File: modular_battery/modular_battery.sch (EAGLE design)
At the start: 16 parts

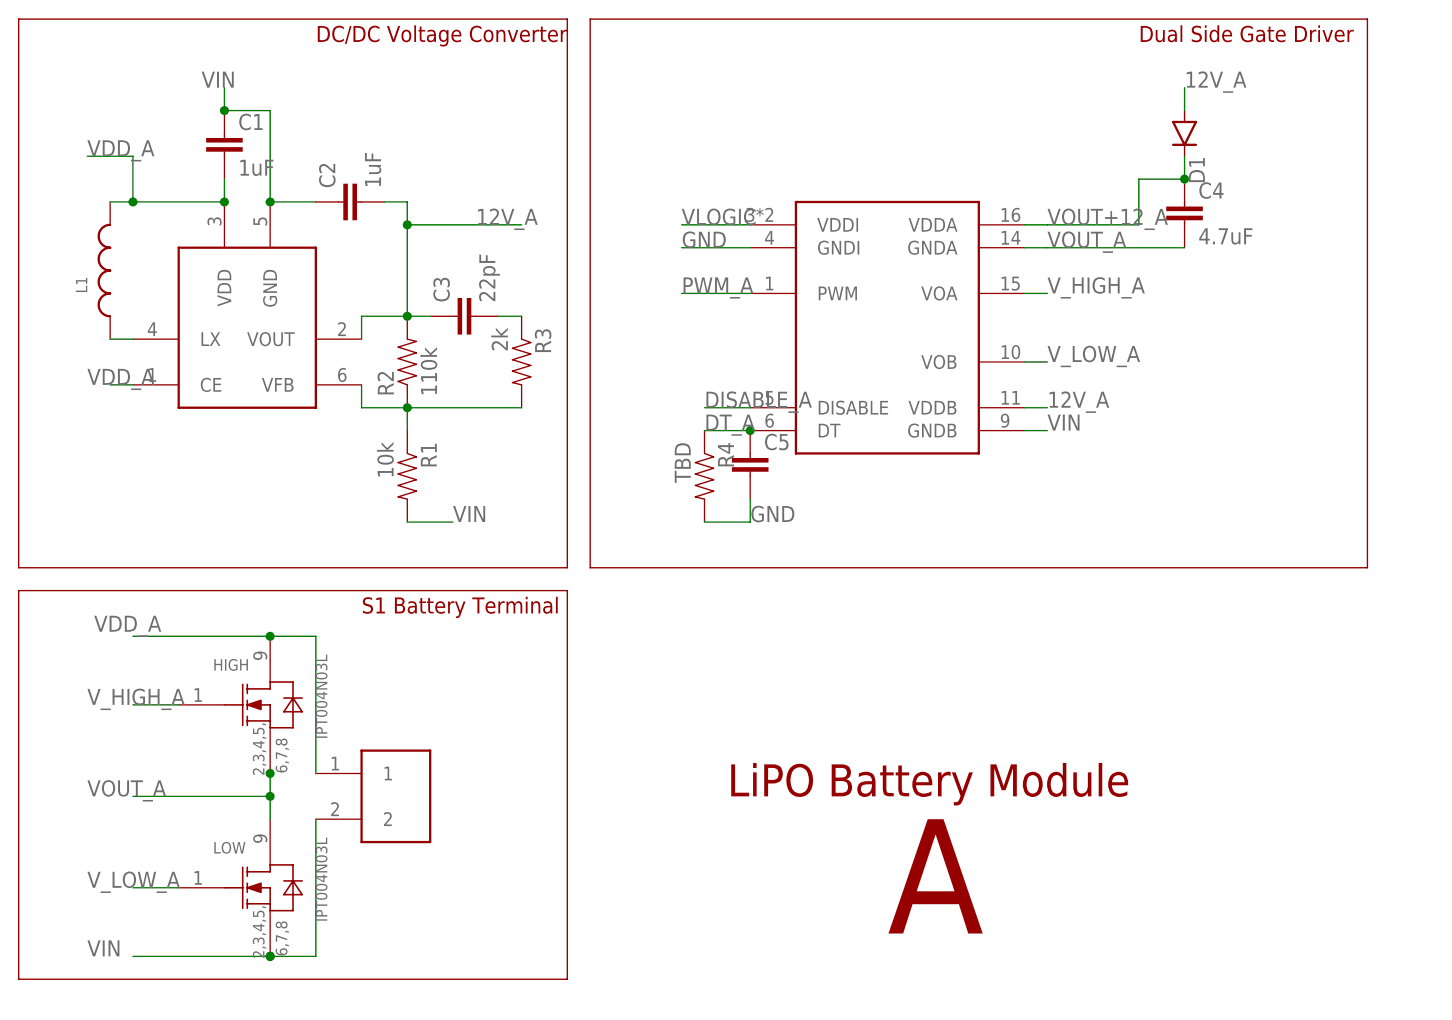
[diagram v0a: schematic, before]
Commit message: added UV supervisor - mosfets look good, copied to modular_battery schematic - i guess you need to recopy it back or something later
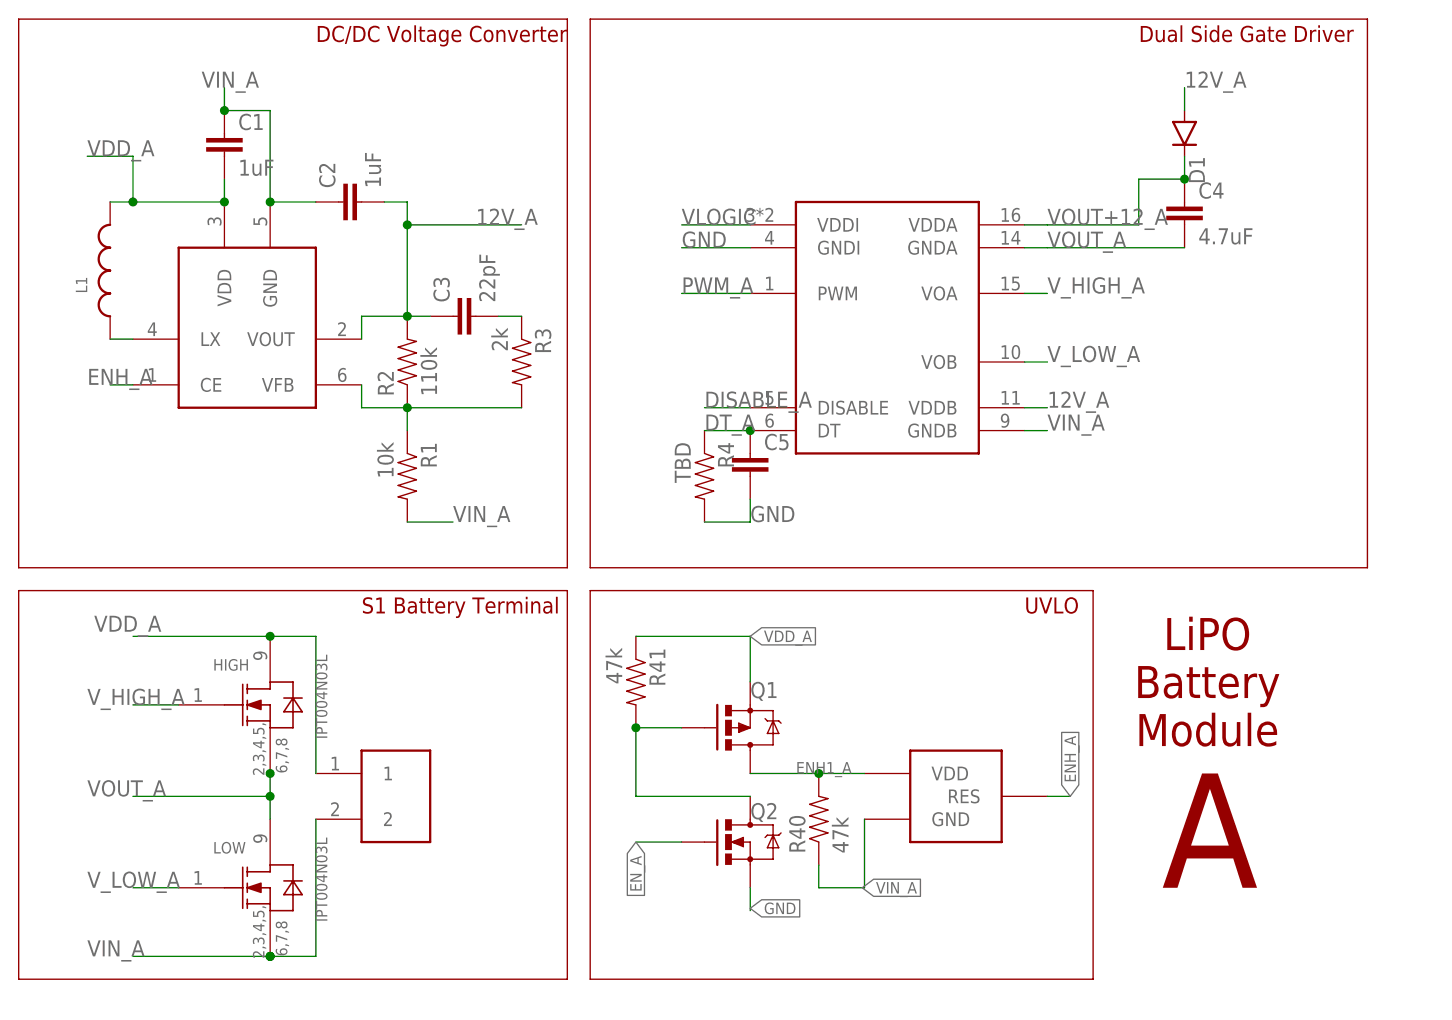
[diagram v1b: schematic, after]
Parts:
- added Q1: MOSFET-PCHANNELSOT223, Custom_old:MOSFET-PCHANNELSOT223
- added Q2: MOSFET-NCHANNELSMD, Custom_old:MOSFET-NCHANNELSMD
- added R40, R41: 47k, SparkFun-Passives:RESISTOR0603-RES
- added U$1: BD49XXK__G, Custom_old:BD49XXK__G
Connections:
- removed net VIN: C1.1, C2.1, LOW.2, LOW.3, LOW.4, LOW.5, LOW.6, LOW.7, LOW.8, R1.2, R1200.GND, SI823.GNDB, U$3.2
- new net ENH1_A: Q1.D, R40.2, U$1.VDD
- new net ENH_A: R1200.CE, U$1.RES
- new net EN_A: Q2.G
- new net N$26: Q1.G, Q2.D, R41.2
- new net VIN_A: C1.1, C2.1, LOW.2, LOW.3, LOW.4, LOW.5, LOW.6, LOW.7, LOW.8, R1.2, R1200.GND, R40.1, SI823.GNDB, U$1.GND, U$3.2
- net GND: now also Q2.S
- net VDD_A: now also Q1.S, R41.1; no longer R1200.CE
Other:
- note added: "UVLO"
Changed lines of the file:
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@@
 <?xml version="1.0" encoding="utf-8"?>
 <!DOCTYPE eagle SYSTEM "eagle.dtd">
-<eagle version="9.2.0">
+<eagle version="9.1.1">
 <drawing>
 <settings>
@@
 <layer number="56" name="wert" color="7" fill="1" visible="no" active="no"/>
 <layer number="57" name="tCAD" color="7" fill="1" visible="no" active="no"/>
+<layer number="59" name="tCarbon" color="7" fill="1" visible="no" active="no"/>
+<layer number="60" name="bCarbon" color="7" fill="1" visible="no" active="no"/>
 <layer number="88" name="SimResults" color="9" fill="1" visible="yes" active="yes"/>
 <layer number="89" name="SimProbes" color="9" fill="1" visible="yes" active="yes"/>
@@
 <layer number="112" name="tSilk" color="7" fill="1" visible="no" active="yes"/>
 <layer number="113" name="ReferenceLS" color="7" fill="1" visible="no" active="no"/>
+<layer number="114" name="Badge_Outline" color="7" fill="1" visible="no" active="yes"/>
+<layer number="115" name="ReferenceISLANDS" color="7" fill="1" visible="no" active="yes"/>
 <layer number="116" name="Patch_BOT" color="9" fill="4" visible="yes" active="yes"/>
+<layer number="117" name="BACKMAAT1" color="7" fill="1" visible="no" active="yes"/>
 <layer number="118" name="Rect_Pads" color="7" fill="1" visible="no" active="no"/>
+<layer number="119" name="KAP_TEKEN" color="7" fill="1" visible="no" active="yes"/>
+<layer number="120" name="KAP_MAAT1" color="7" fill="1" visible="no" active="yes"/>
 <layer number="121" name="_tsilk" color="7" fill="1" visible="yes" active="yes"/>
 <layer number="122" name="_bsilk" color="7" fill="1" visible="yes" active="yes"/>
@@
 <layer number="127" name="_tValues" color="7" fill="1" visible="no" active="yes"/>
 <layer number="128" name="_bValues" color="7" fill="1" visible="no" active="yes"/>
+<layer number="129" name="Mask" color="7" fill="1" visible="no" active="yes"/>
+<layer number="130" name="SMDSTROOK" color="7" fill="1" visible="no" active="yes"/>
 <layer number="131" name="tAdjust" color="7" fill="1" visible="no" active="yes"/>
 <layer number="132" name="bAdjust" color="7" fill="1" visible="no" active="yes"/>
+<layer number="133" name="bottom_silk" color="7" fill="1" visible="no" active="yes"/>
 <layer number="144" name="Drill_legend" color="7" fill="1" visible="yes" active="yes"/>
 <layer number="150" name="Notes" color="7" fill="1" visible="no" active="yes"/>
@@
 <layer number="223" name="223bmp" color="24" fill="1" visible="no" active="no"/>
 <layer number="224" name="224bmp" color="25" fill="1" visible="no" active="no"/>
+<layer number="225" name="225bmp" color="7" fill="1" visible="no" active="yes"/>
+<layer number="226" name="226bmp" color="7" fill="1" visible="no" active="yes"/>
+<layer number="227" name="227bmp" color="7" fill="1" visible="no" active="yes"/>
+<layer number="228" name="228bmp" color="7" fill="1" visible="no" active="yes"/>
+<layer number="229" name="229bmp" color="7" fill="1" visible="no" active="yes"/>
+<layer number="230" name="230bmp" color="7" fill="1" visible="no" active="yes"/>
 <layer number="231" name="Eagle3D_PG1" color="7" fill="1" visible="no" active="no"/>
 <layer number="232" name="Eagle3D_PG2" color="7" fill="1" visible="no" active="no"/>
@@
 <part name="C5" library="SparkFun-Passives" deviceset="CAP" device="0603-CAP"/>
 <part name="L1" library="PowerMagnetics (rev18e)" deviceset="WE-LQS_4025" device="" technology="_74404043220A"/>
+<part name="R40" library="SparkFun-Passives" deviceset="RESISTOR" device="0603-RES" value="47k"/>
+<part name="Q1" library="Custom_old" deviceset="MOSFET-PCHANNEL" device="SOT223"/>
+<part name="R41" library="SparkFun-Passives" deviceset="RESISTOR" device="0603-RES" value="47k"/>
+<part name="Q2" library="Custom_old" deviceset="MOSFET-NCHANNEL" device="SMD"/>
+<part name="U$1" library="Custom_old" deviceset="BD49XX" device="K__G"/>
 </parts>
 <sheets>
@@
 <wire x1="160.02" y1="116.84" x2="73.66" y2="116.84" width="0.1524" layer="94"/>
 <wire x1="73.66" y1="116.84" x2="73.66" y2="177.8" width="0.1524" layer="94"/>
-<text x="88.9" y="91.44" size="3.556" layer="94">LiPO Battery Module</text>
-<text x="106.68" y="76.2" size="12.7" layer="94">A</text>
+<text x="142.24" y="104.14" size="3.556" layer="94" align="center">LiPO
+Battery
+Module</text>
+<text x="137.16" y="81.28" size="12.7" layer="94">A</text>
+<wire x1="73.66" y1="114.3" x2="73.66" y2="71.12" width="0.1524" layer="94"/>
+<wire x1="73.66" y1="71.12" x2="129.54" y2="71.12" width="0.1524" layer="94"/>
+<wire x1="129.54" y1="71.12" x2="129.54" y2="114.3" width="0.1524" layer="94"/>
+<wire x1="129.54" y1="114.3" x2="73.66" y2="114.3" width="0.1524" layer="94"/>
+<text x="121.92" y="111.76" size="1.778" layer="94">UVLO</text>
 </plain>
 <instances>
@@
 <attribute name="VALUE" x="22.86" y="147.32" size="1.27" layer="96" rot="R90"/>
 </instance>
+<instance part="R40" gate="G$1" x="99.06" y="88.9" rot="R90">
+<attribute name="NAME" x="97.5614" y="85.09" size="1.778" layer="95" rot="R90"/>
+<attribute name="VALUE" x="102.362" y="85.09" size="1.778" layer="96" rot="R90"/>
+</instance>
+<instance part="Q1" gate="G$1" x="91.44" y="99.06" smashed="yes" rot="MR180">
+<attribute name="NAME" x="91.44" y="104.14" size="1.778" layer="95" rot="MR180"/>
+</instance>
+<instance part="R41" gate="G$1" x="78.74" y="104.14" rot="R270">
+<attribute name="NAME" x="80.2386" y="107.95" size="1.778" layer="95" rot="R270"/>
+<attribute name="VALUE" x="75.438" y="107.95" size="1.778" layer="96" rot="R270"/>
+</instance>
+<instance part="Q2" gate="G$1" x="91.44" y="86.36" smashed="yes">
+<attribute name="NAME" x="91.44" y="88.9" size="1.778" layer="95"/>
+</instance>
+<instance part="U$1" gate="G$1" x="114.3" y="91.44"/>
 </instances>
 <busses>
@@
 <wire x1="91.44" y1="121.92" x2="86.36" y2="121.92" width="0.1524" layer="91"/>
 <label x="91.44" y="121.92" size="1.778" layer="95"/>
+</segment>
+<segment>
+<pinref part="Q2" gate="G$1" pin="S"/>
+<wire x1="91.44" y1="81.28" x2="91.44" y2="78.74" width="0.1524" layer="91"/>
+<label x="91.44" y="78.994" size="1.27" layer="95" xref="yes"/>
 </segment>
 </net>
@@
 </segment>
 <segment>
-<pinref part="R1200" gate="G$1" pin="CE"/>
-<wire x1="22.86" y1="137.16" x2="20.32" y2="137.16" width="0.1524" layer="91"/>
-<label x="17.78" y="137.16" size="1.778" layer="95"/>
+<pinref part="Q1" gate="G$1" pin="S"/>
+<wire x1="91.44" y1="104.14" x2="91.44" y2="109.22" width="0.1524" layer="91"/>
+<label x="91.44" y="109.22" size="1.27" layer="95" xref="yes"/>
+<pinref part="R41" gate="G$1" pin="1"/>
+<wire x1="78.74" y1="109.22" x2="91.44" y2="109.22" width="0.1524" layer="91"/>
 </segment>
 </net>
@@
 </segment>
 </net>
-<net name="VIN" class="0">
+<net name="VIN_A" class="0">
 <segment>
 <wire x1="38.1" y1="73.66" x2="22.86" y2="73.66" width="0.1524" layer="91"/>
@@
 <junction x="38.1" y="157.48"/>
 </segment>
+<segment>
+<pinref part="R40" gate="G$1" pin="1"/>
+<wire x1="99.06" y1="83.82" x2="99.06" y2="81.28" width="0.1524" layer="91"/>
+<label x="103.886" y="81.28" size="1.27" layer="95" xref="yes"/>
+<pinref part="U$1" gate="G$1" pin="GND"/>
+<wire x1="104.14" y1="88.9" x2="104.14" y2="81.28" width="0.1524" layer="91"/>
+<wire x1="104.14" y1="81.28" x2="99.06" y2="81.28" width="0.1524" layer="91"/>
+</segment>
 </net>
 <net name="PWM_A" class="0">
@@
 </segment>
 </net>
+<net name="N$26" class="0">
+<segment>
+<pinref part="R41" gate="G$1" pin="2"/>
+<pinref part="Q1" gate="G$1" pin="G"/>
+<wire x1="78.74" y1="99.06" x2="83.82" y2="99.06" width="0.1524" layer="91"/>
+<pinref part="Q2" gate="G$1" pin="D"/>
+<wire x1="91.44" y1="91.44" x2="78.74" y2="91.44" width="0.1524" layer="91"/>
+<wire x1="78.74" y1="91.44" x2="78.74" y2="99.06" width="0.1524" layer="91"/>
+<junction x="78.74" y="99.06"/>
+</segment>
+</net>
+<net name="EN_A" class="0">
+<segment>
+<pinref part="Q2" gate="G$1" pin="G"/>
+<wire x1="83.82" y1="86.36" x2="78.74" y2="86.36" width="0.1524" layer="91"/>
+<label x="78.74" y="86.36" size="1.27" layer="95" rot="R270" xref="yes"/>
+</segment>
+</net>
+<net name="ENH1_A" class="0">
+<segment>
+<pinref part="Q1" gate="G$1" pin="D"/>
+<wire x1="91.44" y1="93.98" x2="99.06" y2="93.98" width="0.1524" layer="91"/>
+<pinref part="R40" gate="G$1" pin="2"/>
+<wire x1="99.06" y1="93.98" x2="104.14" y2="93.98" width="0.1524" layer="91"/>
+<junction x="99.06" y="93.98"/>
+<label x="96.52" y="93.98" size="1.27" layer="95"/>
+<pinref part="U$1" gate="G$1" pin="VDD"/>
+</segment>
+</net>
+<net name="ENH_A" class="0">
+<segment>
+<pinref part="U$1" gate="G$1" pin="RES"/>
+<wire x1="124.46" y1="91.44" x2="127" y2="91.44" width="0.1524" layer="91"/>
+<label x="127" y="91.44" size="1.27" layer="95" rot="R90" xref="yes"/>
+</segment>
+<segment>
+<pinref part="R1200" gate="G$1" pin="CE"/>
+<wire x1="22.86" y1="137.16" x2="20.32" y2="137.16" width="0.1524" layer="91"/>
+<label x="17.78" y="137.16" size="1.778" layer="95"/>
+</segment>
+</net>
 </nets>
 </sheet>
@@
 </schematic>
 </drawing>
+<compatibility>
+<note version="6.3" minversion="6.2.2" severity="warning">
+Since Version 6.2.2 text objects can contain more than one line,
+which will not be processed correctly with this version.
+</note>
+</compatibility>
 </eagle>

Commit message: final board layout?
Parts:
- removed HIGH, LOW: IPT004N03L, IPT004N03L:IPT004N03L
- removed Q1: MOSFET-PCHANNELSOT223, Custom_old:MOSFET-PCHANNELSOT223
- removed Q2: MOSFET-NCHANNELSMD, Custom_old:MOSFET-NCHANNELSMD
- removed R1200: R1200SOT-23-6, Custom_old:R1200SOT-23-6
- removed R40, R41: 47k, SparkFun-Passives:RESISTOR0603-RES
- removed SI823: SI8231SOIC16W, Custom_old:SI8231SOIC16W
- removed U$1: BD49XXK__G, Custom_old:BD49XXK__G
- added DRIVER1: SI8231SOIC16W, Custom_old:SI8231SOIC16W
- added NMOS1, NMOS2: IPT004N03L, IPT004N03L:IPT004N03L
- added NMOS3: MOSFET-NCHANNELSMD, Custom_old:MOSFET-NCHANNELSMD
- added PMOS1: MOSFET-PCHANNELSOT223, Custom_old:MOSFET-PCHANNELSOT223
- added R5, R6: 47k, SparkFun-Passives:RESISTOR0603-RES
- added VDETECTOR1: BD49XXK__G, Custom_old:BD49XXK__G
- added VREG1: R1200SOT-23-6, Custom_old:R1200SOT-23-6
- R4: value TBD -> 1k
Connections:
- net 12V_A: now also DRIVER1.VDDB, VREG1.VOUT; no longer R1200.VOUT, SI823.VDDB
- net DISABLE_A: now also DRIVER1.DISABLE; no longer SI823.DISABLE
- net DT_A: now also DRIVER1.DT; no longer SI823.DT
- net ENH1_A: now also PMOS1.D, R5.2, VDETECTOR1.VDD; no longer Q1.D, R40.2, U$1.VDD
- net ENH_A: now also VDETECTOR1.RES, VREG1.CE; no longer R1200.CE, U$1.RES
- net EN_A: now also NMOS3.G; no longer Q2.G
- net GND: now also DRIVER1.GNDI, NMOS3.S; no longer Q2.S, SI823.GNDI
- net N$1: now also VREG1.LX; no longer R1200.LX
- net N$26: now also NMOS3.D, PMOS1.G, R6.2; no longer Q1.G, Q2.D, R41.2
- net N$3: now also VREG1.VFB; no longer R1200.VFB
- net PWM_A: now also DRIVER1.PWM; no longer SI823.PWM
- net VDD_A: now also NMOS1.9, PMOS1.S, R6.1, VREG1.VDD; no longer HIGH.9, Q1.S, R1200.VDD, R41.1
- net VIN_A: now also DRIVER1.GNDB, NMOS2.2, NMOS2.3, NMOS2.4, NMOS2.5, NMOS2.6, NMOS2.7, NMOS2.8, R5.1, VDETECTOR1.GND, VREG1.GND; no longer LOW.2, LOW.3, LOW.4, LOW.5, LOW.6, LOW.7, LOW.8, R1200.GND, R40.1, SI823.GNDB, U$1.GND
- net VLOGIC: now also DRIVER1.VDDI; no longer SI823.VDDI
- net VOUT+12_A: now also DRIVER1.VDDA; no longer SI823.VDDA
- net VOUT_A: now also DRIVER1.GNDA, NMOS1.2, NMOS1.3, NMOS1.4, NMOS1.5, NMOS1.6, NMOS1.7, NMOS1.8, NMOS2.9; no longer HIGH.2, HIGH.3, HIGH.4, HIGH.5, HIGH.6, HIGH.7, HIGH.8, LOW.9, SI823.GNDA
- net V_HIGH_A: now also DRIVER1.VOA, NMOS1.1; no longer HIGH.1, SI823.VOA
- net V_LOW_A: now also DRIVER1.VOB, NMOS2.1; no longer LOW.1, SI823.VOB
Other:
- moved on the sheet: C1, C2, C3, C4, C5, D1, L1, R1, R2, R3, R4
